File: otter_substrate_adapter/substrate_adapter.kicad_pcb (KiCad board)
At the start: 2 copper layers, 25.4 x 25.4 mm, 18 parts, among them J1 PIX1, J10 R_CONN, J11 PIX1, J12 PIX2, J13 PIX3, J14 BOT_TCE, J15 TOP_TCE, J16 PIX4, J17 PIX5, J18 PIX6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

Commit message: reduce otter pin drill hole diameter
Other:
- board text added: "dc568a0"
- board text removed: "45f1e60"

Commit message: update silk
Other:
- board text added: "c0adfdf"
- board text removed: "dc568a0"
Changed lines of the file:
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@@
     )
   )
-  (gr_text dc568a0 (at -7 12) (layer B.SilkS)
+  (gr_text c0adfdf (at -7 12) (layer B.SilkS)
     (effects (font (size 1 1) (thickness 0.15)) (justify mirror))
   )
-  (gr_text dc568a0 (at -7 12) (layer F.SilkS)
+  (gr_text c0adfdf (at -7 12) (layer F.SilkS)
     (effects (font (size 1 1) (thickness 0.15)))
   )

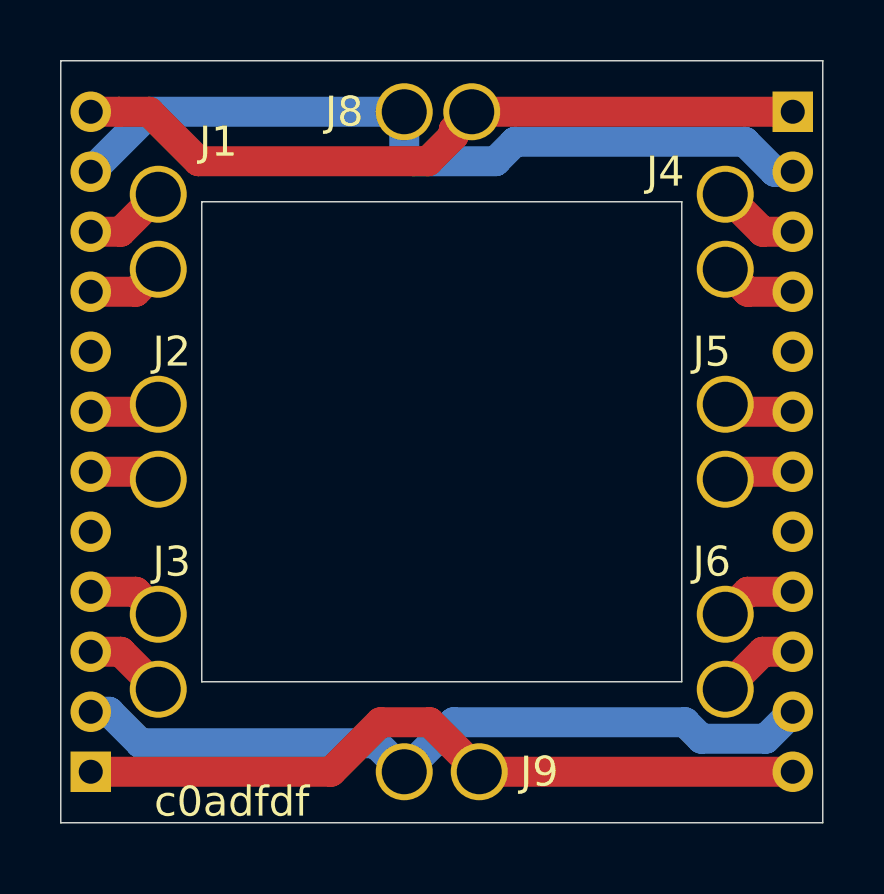
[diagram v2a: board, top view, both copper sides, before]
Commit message: update spring pin hole size and improve crossbar routing
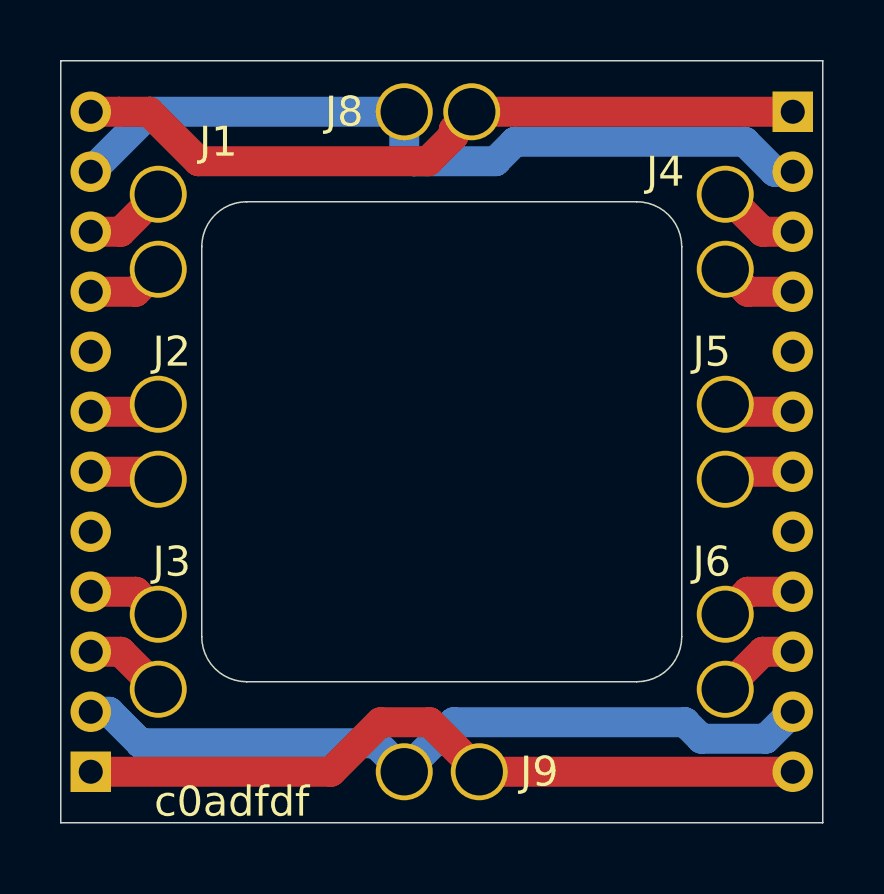
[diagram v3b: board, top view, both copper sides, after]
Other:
- outline, holes or cut-outs redrawn
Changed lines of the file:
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@@
   (general
     (thickness 1.6)
-    (drawings 10)
+    (drawings 14)
     (tracks 57)
     (zones 0)
@@
       (effects (font (size 1 1) (thickness 0.15)))
     )
-    (pad 1 thru_hole circle (at 0 0 90) (size 1.9 1.9) (drill 1.5) (layers *.Cu *.Mask)
+    (pad 1 thru_hole circle (at 0 0 90) (size 1.9 1.9) (drill 1.58) (layers *.Cu *.Mask)
       (net 1 "Net-(J1-Pad1)"))
     (model ${KIPRJMOD}/../3d/mill-max-0964-0-15-20-85-14-11-0.step
@@
       (effects (font (size 1 1) (thickness 0.15)))
     )
-    (pad 1 thru_hole circle (at 0 0 90) (size 1.9 1.9) (drill 1.5) (layers *.Cu *.Mask)
+    (pad 1 thru_hole circle (at 0 0 90) (size 1.9 1.9) (drill 1.58) (layers *.Cu *.Mask)
       (net 2 "Net-(J2-Pad1)"))
     (model ${KIPRJMOD}/../3d/mill-max-0964-0-15-20-85-14-11-0.step
@@
       (effects (font (size 1 1) (thickness 0.15)))
     )
-    (pad 1 thru_hole circle (at 0 0 90) (size 1.9 1.9) (drill 1.5) (layers *.Cu *.Mask)
+    (pad 1 thru_hole circle (at 0 0 90) (size 1.9 1.9) (drill 1.58) (layers *.Cu *.Mask)
       (net 3 "Net-(J3-Pad1)"))
     (model ${KIPRJMOD}/../3d/mill-max-0964-0-15-20-85-14-11-0.step
@@
       (effects (font (size 1 1) (thickness 0.15)))
     )
-    (pad 1 thru_hole circle (at 0 0 90) (size 1.9 1.9) (drill 1.5) (layers *.Cu *.Mask)
+    (pad 1 thru_hole circle (at 0 0 90) (size 1.9 1.9) (drill 1.58) (layers *.Cu *.Mask)
       (net 4 "Net-(J10-Pad3)"))
     (model ${KIPRJMOD}/../3d/mill-max-0964-0-15-20-85-14-11-0.step
@@
       (effects (font (size 1 1) (thickness 0.15)))
     )
-    (pad 1 thru_hole circle (at 0 0 90) (size 1.9 1.9) (drill 1.5) (layers *.Cu *.Mask)
+    (pad 1 thru_hole circle (at 0 0 90) (size 1.9 1.9) (drill 1.58) (layers *.Cu *.Mask)
       (net 5 "Net-(J10-Pad6)"))
     (model ${KIPRJMOD}/../3d/mill-max-0964-0-15-20-85-14-11-0.step
@@
       (effects (font (size 1 1) (thickness 0.15)))
     )
-    (pad 1 thru_hole circle (at 0 0 90) (size 1.9 1.9) (drill 1.5) (layers *.Cu *.Mask)
+    (pad 1 thru_hole circle (at 0 0 90) (size 1.9 1.9) (drill 1.58) (layers *.Cu *.Mask)
       (net 6 "Net-(J10-Pad9)"))
     (model ${KIPRJMOD}/../3d/mill-max-0964-0-15-20-85-14-11-0.step
@@
       (effects (font (size 1 1) (thickness 0.15)))
     )
-    (pad 1 thru_hole circle (at 0 0 90) (size 1.9 1.9) (drill 1.5) (layers *.Cu *.Mask)
+    (pad 1 thru_hole circle (at 0 0 90) (size 1.9 1.9) (drill 1.58) (layers *.Cu *.Mask)
       (net 12 "Net-(J10-Pad2)"))
     (model ${KIPRJMOD}/../3d/mill-max-0964-0-15-20-85-14-11-0.step
@@
       (effects (font (size 1 1) (thickness 0.15)))
     )
-    (pad 1 thru_hole circle (at 0 0 90) (size 1.9 1.9) (drill 1.5) (layers *.Cu *.Mask)
+    (pad 1 thru_hole circle (at 0 0 90) (size 1.9 1.9) (drill 1.58) (layers *.Cu *.Mask)
       (net 7 "Net-(J10-Pad12)"))
     (model ${KIPRJMOD}/../3d/mill-max-0964-0-15-20-85-14-11-0.step
@@
       (effects (font (size 1 1) (thickness 0.15)))
     )
-    (pad 1 thru_hole circle (at 0 0 90) (size 1.9 1.9) (drill 1.5) (layers *.Cu *.Mask)
+    (pad 1 thru_hole circle (at 0 0 90) (size 1.9 1.9) (drill 1.58) (layers *.Cu *.Mask)
       (net 11 "Net-(J11-Pad1)"))
     (model ${KIPRJMOD}/../3d/mill-max-0964-0-15-20-85-14-11-0.step
@@
       (effects (font (size 1 1) (thickness 0.15)))
     )
-    (pad 1 thru_hole circle (at 0 0 90) (size 1.9 1.9) (drill 1.5) (layers *.Cu *.Mask)
+    (pad 1 thru_hole circle (at 0 0 90) (size 1.9 1.9) (drill 1.58) (layers *.Cu *.Mask)
       (net 10 "Net-(J12-Pad1)"))
     (model ${KIPRJMOD}/../3d/mill-max-0964-0-15-20-85-14-11-0.step
@@
       (effects (font (size 1 1) (thickness 0.15)))
     )
-    (pad 1 thru_hole circle (at 0 0 90) (size 1.9 1.9) (drill 1.5) (layers *.Cu *.Mask)
+    (pad 1 thru_hole circle (at 0 0 90) (size 1.9 1.9) (drill 1.58) (layers *.Cu *.Mask)
       (net 9 "Net-(J13-Pad1)"))
     (model ${KIPRJMOD}/../3d/mill-max-0964-0-15-20-85-14-11-0.step
@@
       (effects (font (size 1 1) (thickness 0.15)))
     )
-    (pad 1 thru_hole circle (at 0 0 90) (size 1.9 1.9) (drill 1.5) (layers *.Cu *.Mask)
+    (pad 1 thru_hole circle (at 0 0 90) (size 1.9 1.9) (drill 1.58) (layers *.Cu *.Mask)
       (net 8 "Net-(J10-Pad11)"))
     (model ${KIPRJMOD}/../3d/mill-max-0964-0-15-20-85-14-11-0.step
@@
       (effects (font (size 1 1) (thickness 0.15)))
     )
-    (pad 1 thru_hole circle (at 0 0 90) (size 1.9 1.9) (drill 1.5) (layers *.Cu *.Mask)
+    (pad 1 thru_hole circle (at 0 0 90) (size 1.9 1.9) (drill 1.58) (layers *.Cu *.Mask)
       (net 13 "Net-(J10-Pad1)"))
     (model ${KIPRJMOD}/../3d/mill-max-0964-0-15-20-85-14-11-0.step
@@
       (effects (font (size 1 1) (thickness 0.15)))
     )
-    (pad 1 thru_hole circle (at 0 0 90) (size 1.9 1.9) (drill 1.5) (layers *.Cu *.Mask)
+    (pad 1 thru_hole circle (at 0 0 90) (size 1.9 1.9) (drill 1.58) (layers *.Cu *.Mask)
       (net 16 "Net-(J10-Pad4)"))
     (model ${KIPRJMOD}/../3d/mill-max-0964-0-15-20-85-14-11-0.step
@@
       (effects (font (size 1 1) (thickness 0.15)))
     )
-    (pad 1 thru_hole circle (at 0 0 90) (size 1.9 1.9) (drill 1.5) (layers *.Cu *.Mask)
+    (pad 1 thru_hole circle (at 0 0 90) (size 1.9 1.9) (drill 1.58) (layers *.Cu *.Mask)
       (net 15 "Net-(J10-Pad7)"))
     (model ${KIPRJMOD}/../3d/mill-max-0964-0-15-20-85-14-11-0.step
@@
       (effects (font (size 1 1) (thickness 0.15)))
     )
-    (pad 1 thru_hole circle (at 0 0 90) (size 1.9 1.9) (drill 1.5) (layers *.Cu *.Mask)
+    (pad 1 thru_hole circle (at 0 0 90) (size 1.9 1.9) (drill 1.58) (layers *.Cu *.Mask)
       (net 14 "Net-(J10-Pad10)"))
     (model ${KIPRJMOD}/../3d/mill-max-0964-0-15-20-85-14-11-0.step
@@
     )
   )
+  (gr_arc (start 6.5 -6.5) (end 8 -6.5) (angle -90) (layer Edge.Cuts) (width 0.05))
+  (gr_arc (start -6.5 -6.5) (end -6.5 -8) (angle -90) (layer Edge.Cuts) (width 0.05))
+  (gr_arc (start -6.5 6.5) (end -8 6.5) (angle -90) (layer Edge.Cuts) (width 0.05))
+  (gr_arc (start 6.5 6.5) (end 6.5 8) (angle -90) (layer Edge.Cuts) (width 0.05))
   (gr_text c0adfdf (at -7 12) (layer B.SilkS)
     (effects (font (size 1 1) (thickness 0.15)) (justify mirror))
@@
     (effects (font (size 1 1) (thickness 0.15)))
   )
-  (gr_line (start 8 8) (end -8 8) (layer Edge.Cuts) (width 0.05))
-  (gr_line (start 8 -8) (end 8 8) (layer Edge.Cuts) (width 0.05))
-  (gr_line (start -8 -8) (end 8 -8) (layer Edge.Cuts) (width 0.05))
-  (gr_line (start -8 8) (end -8 -8) (layer Edge.Cuts) (width 0.05))
+  (gr_line (start 6.5 8) (end -6.5 8) (layer Edge.Cuts) (width 0.05))
+  (gr_line (start 8 -6.5) (end 8 6.5) (layer Edge.Cuts) (width 0.05))
+  (gr_line (start -6.5 -8) (end 6.5 -8) (layer Edge.Cuts) (width 0.05))
+  (gr_line (start -8 6.5) (end -8 -6.5) (layer Edge.Cuts) (width 0.05))
   (gr_line (start -12.7 -12.7) (end -12.7 12.7) (layer Edge.Cuts) (width 0.05))
   (gr_line (start 12.7 -12.7) (end -12.7 -12.7) (layer Edge.Cuts) (width 0.05))

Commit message: update silk
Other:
- board text added: "365180b"
- board text removed: "c0adfdf"
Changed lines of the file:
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@@
   (gr_arc (start -6.5 6.5) (end -8 6.5) (angle -90) (layer Edge.Cuts) (width 0.05))
   (gr_arc (start 6.5 6.5) (end 6.5 8) (angle -90) (layer Edge.Cuts) (width 0.05))
-  (gr_text c0adfdf (at -7 12) (layer B.SilkS)
+  (gr_text 365180b (at -7 12) (layer B.SilkS)
     (effects (font (size 1 1) (thickness 0.15)) (justify mirror))
   )
-  (gr_text c0adfdf (at -7 12) (layer F.SilkS)
+  (gr_text 365180b (at -7 12) (layer F.SilkS)
     (effects (font (size 1 1) (thickness 0.15)))
   )
